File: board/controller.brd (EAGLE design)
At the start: 100 x 100 mm, 70 parts, among them J1 X, J10 FEED_HOLD, J11 PROBE, J12 ERROR, J13 HOLDING, J14 GND, J15 MOTOR_CURRENT, J16 SD_READER, J17 WHEEL, J18 FEED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

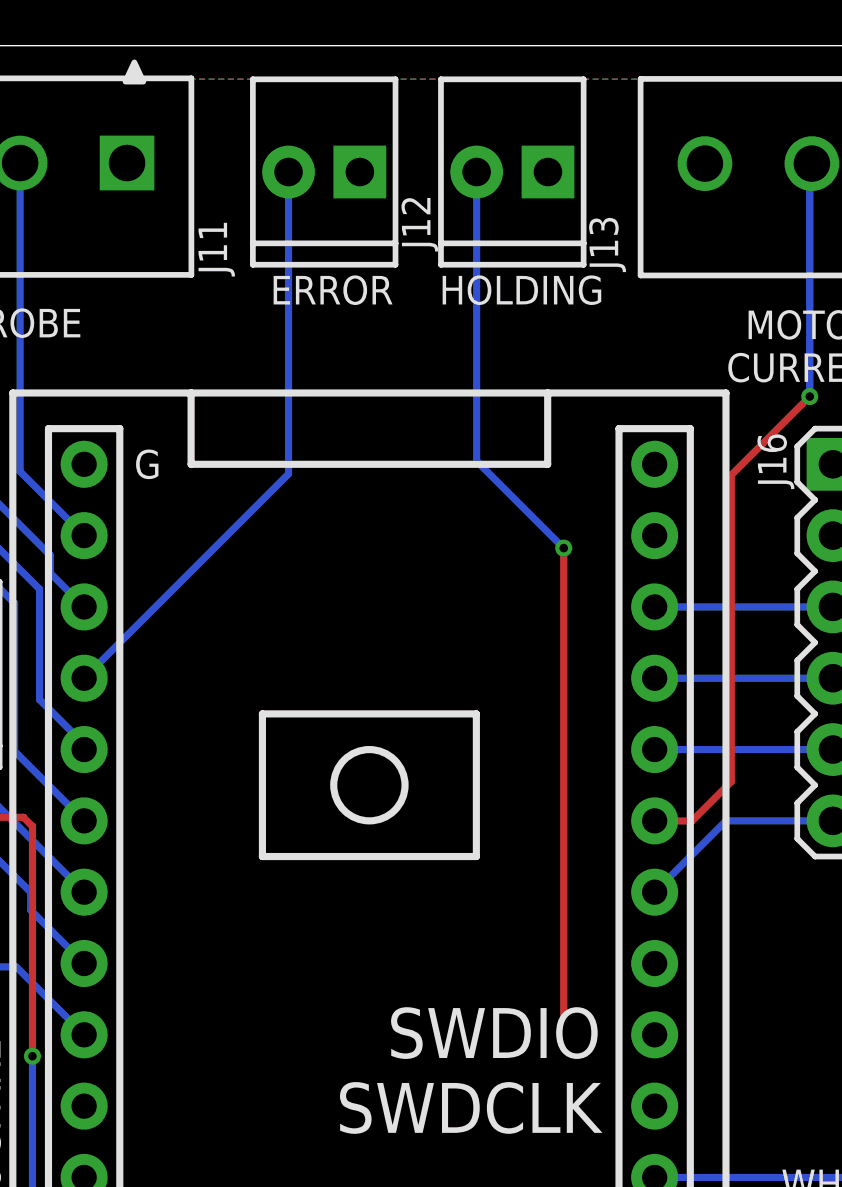
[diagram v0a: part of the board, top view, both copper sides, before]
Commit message: added currect limit resistors for holding and error control panel leds added alarm string to control panel display if in alarm state, hitting any control panel key clears alarm without reseting
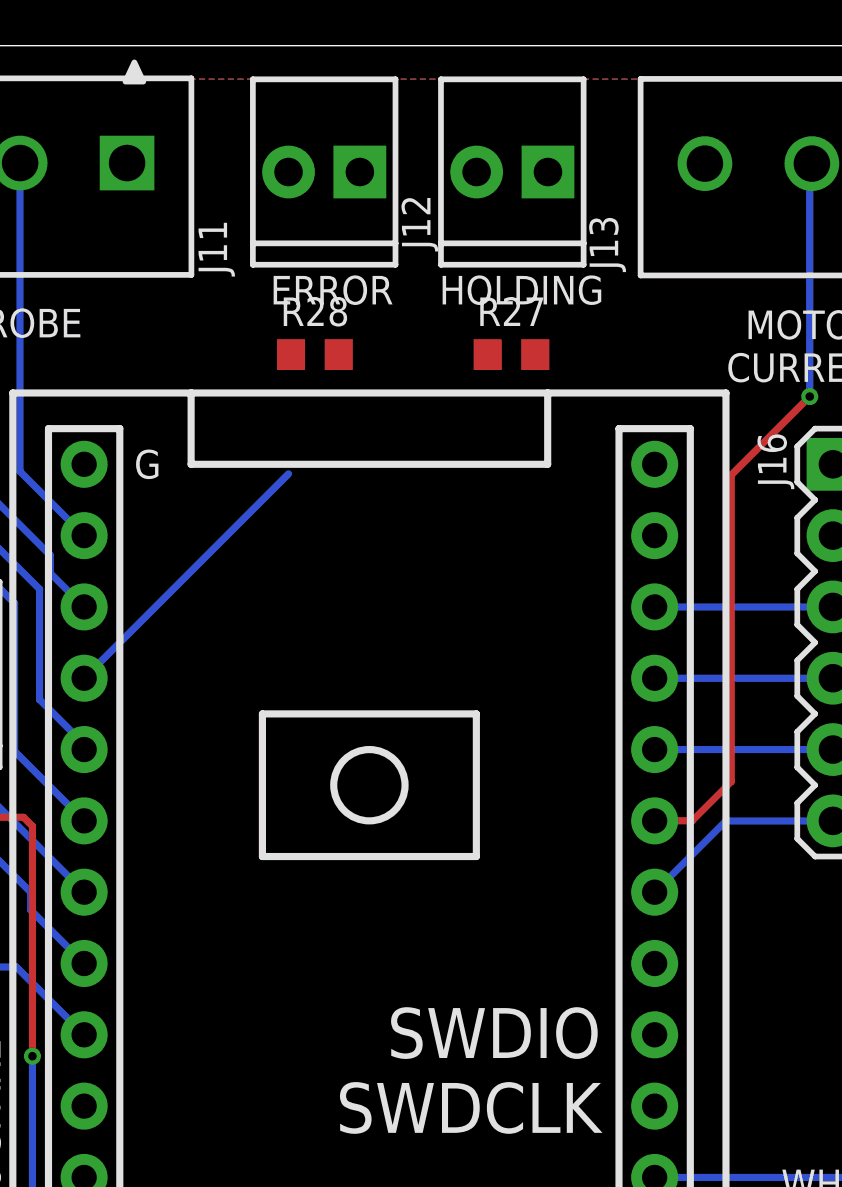
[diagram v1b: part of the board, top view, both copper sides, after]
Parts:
- added R27, R28: 220, holla:R0603
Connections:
- new net N$12: J13.2, R27.1
- new net N$13: J12.2, R28.1
- net ERROR_INDICATOR_OUT: now also R28.2; no longer J12.2
- net FEED_HOLDING_OUT: now also R27.2; no longer J13.2
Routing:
- net FEED_HOLDING_OUT: track 31.3 -> 0.00 mm, vias 1 -> 0
- net ERROR_INDICATOR_OUT: track 21.0 -> 10.3 mm
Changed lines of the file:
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@@
 <attribute name="VALUE" x="1.1415" y="20.887" size="1.27" layer="27" font="vector"/>
+</element>
+<element name="R27" library="holla" package="R0603" value="220" x="33" y="89">
+<attribute name="DESC" value="5%" x="33" y="89" size="1.778" layer="27" display="off"/>
+</element>
+<element name="R28" library="holla" package="R0603" value="220" x="26" y="89">
+<attribute name="DESC" value="5%" x="26" y="89" size="1.778" layer="27" display="off"/>
 </element>
 </elements>
@@
 </signal>
 <signal name="ERROR_INDICATOR_OUT">
-<contactref element="J12" pad="2"/>
 <contactref element="U2" pad="3.2"/>
-<wire x1="25.06" y1="95.5" x2="25.06" y2="84.75" width="0.254" layer="16"/>
 <wire x1="25.06" y1="84.75" x2="17.78" y2="77.47" width="0.254" layer="16"/>
+<contactref element="R28" pad="2"/>
+<wire x1="26.85" y1="89" x2="17.78" y2="77.47" width="0" layer="19" extent="1-1"/>
 </signal>
 <signal name="FEED_HOLDING_OUT">
-<contactref element="J13" pad="2"/>
-<wire x1="31.76" y1="95.5" x2="31.76" y2="85.207" width="0.254" layer="16"/>
-<wire x1="31.76" y1="85.207" x2="34.8615" y2="82.1055" width="0.254" layer="16"/>
-<via x="34.8615" y="82.1055" extent="1-16" drill="0.3048"/>
-<wire x1="34.8615" y1="82.1055" x2="34.8615" y2="65.4685" width="0.254" layer="1"/>
 <contactref element="U2" pad="1.2"/>
-<wire x1="34.8615" y1="65.4685" x2="38.1" y2="67.31" width="0" layer="19" extent="1-1"/>
+<contactref element="R27" pad="2"/>
+<wire x1="33.85" y1="89" x2="38.1" y2="67.31" width="0" layer="19" extent="1-1"/>
 </signal>
 <signal name="Z_DISPLAY_RX_IN">
@@
 <contactref element="J5" pad="3"/>
 </signal>
+<signal name="N$12">
+<contactref element="J13" pad="2"/>
+<contactref element="R27" pad="1"/>
+<wire x1="32.15" y1="89" x2="31.76" y2="95.5" width="0" layer="19" extent="1-1"/>
+</signal>
+<signal name="N$13">
+<contactref element="J12" pad="2"/>
+<contactref element="R28" pad="1"/>
+<wire x1="25.15" y1="89" x2="25.06" y2="95.5" width="0" layer="19" extent="1-1"/>
+</signal>
 </signals>

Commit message: sch     added a couple values so charm.ulp would place ICs
makefile
    moved so vim's ctrl-m would make project

src
    not using G92 anymore, just setting selected coordinate system using hyatt_zero_offset_x,y from grbl settings #33 and #34
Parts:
- R7, R8: value 2.2k -> 1k
- U3, U4: value (none) -> MCP23017
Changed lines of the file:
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@@
 <elements>
 <element name="U2" library="holla" package="BOARD-PSOC-CY8CKIT-059" value="" x="27.94" y="53.34" smashed="yes" rot="R180"/>
-<element name="U3" library="holla" package="SO28W" value="" x="85.03" y="85.146" smashed="yes" rot="R180">
+<element name="U3" library="holla" package="SO28W" value="MCP23017" x="85.03" y="85.146" smashed="yes" rot="R180">
 <attribute name="MPN" value="MCP23017-E/SO" x="85.03" y="85.146" size="1.778" layer="27" rot="R180" display="off"/>
 <attribute name="OC_NEWARK" value="31K2958" x="85.03" y="85.146" size="1.778" layer="27" rot="R180" display="off"/>
@@
 <attribute name="VALUE" x="73.473" y="89.21" size="1.778" layer="27" ratio="10" rot="R270"/>
 </element>
-<element name="U4" library="holla" package="SO28W" value="" x="85.11" y="24.546" smashed="yes" rot="R180">
+<element name="U4" library="holla" package="SO28W" value="MCP23017" x="85.11" y="24.546" smashed="yes" rot="R180">
 <attribute name="MPN" value="MCP23017-E/SO" x="85.11" y="24.546" size="1.778" layer="27" rot="R180" display="off"/>
 <attribute name="OC_NEWARK" value="31K2958" x="85.11" y="24.546" size="1.778" layer="27" rot="R180" display="off"/>
@@
 <attribute name="VALUE" x="83.622" y="31.07" size="1.016" layer="27" ratio="21" align="top-center"/>
 </element>
-<element name="R8" library="holla" package="R0603" value="2.2k" x="69.159" y="91.552" smashed="yes" rot="R180">
+<element name="R8" library="holla" package="R0603" value="1k" x="69.159" y="91.552" smashed="yes" rot="R180">
 <attribute name="DESC" value="5%" x="69.159" y="91.552" size="1.778" layer="27" rot="R180" display="off"/>
 <attribute name="NAME" x="66.459" y="92.136" size="1.016" layer="25" ratio="21" rot="R180" align="bottom-center"/>
 <attribute name="VALUE" x="69.159" y="92.568" size="1.016" layer="27" ratio="21" rot="R180" align="top-center"/>
 </element>
-<element name="R7" library="holla" package="R0603" value="2.2k" x="69.159" y="94.401" smashed="yes" rot="R180">
+<element name="R7" library="holla" package="R0603" value="1k" x="69.159" y="94.401" smashed="yes" rot="R180">
 <attribute name="DESC" value="5%" x="69.159" y="94.401" size="1.778" layer="27" rot="R180" display="off"/>
 <attribute name="NAME" x="66.359" y="94.985" size="1.016" layer="25" ratio="21" rot="R180" align="bottom-center"/>
